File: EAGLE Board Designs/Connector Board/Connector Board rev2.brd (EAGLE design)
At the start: 109.2 x 45.7 mm, 51 parts, among them J1 CONNECTOR-8_μF_T_V_BLACK, J10 CONNECTOR-16_MF_T_V_, J11 CONNECTOR-18_MF_T_V_, J12 CONNECTOR-8_μF_T_V_BLACK, J2 CONNECTOR-8_μF_T_V_BLACK, J3 CONNECTOR-8_μF_T_V_BLACK, J4 CONNECTOR-10_MF_T_V_, J5 CONNECTOR-4_μF_T_V_BLACK, J6 CONNECTOR-24_CONNECTOR-24_, J7 CONNECTOR-24_CONNECTOR-24_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

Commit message: awaiting sab connections
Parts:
- removed R1, R2, R3: RESISTOR_0603_100, HyTechDevices:0603-RES
- removed R14, R15: RESISTOR_0603_100K, HyTechDevices:0603-RES
- removed TP3, TP4: TEST_POINT, HyTechDevices:5015
- added J13: CONNECTOR-2_MF_T_V_, HyTechDevices - Copy:MOLEX_MICROFIT_PTH_VERTICAL_02_SINGLE
- added JP1, JP2: JUMPER_0603_, HyTechDevices:0603-RES
- J1: value CONNECTOR-8_μF_T_V_BLACK -> CONNECTOR-6_μF_T_V_BLACK; device HyTechDevices:MOLEX_MICROFIT_PTH_VERTICAL_08_DUAL -> HyTechDevices:MOLEX_MICROFIT_PTH_VERTICAL_06_DUAL
- J4: value CONNECTOR-10_MF_T_V_ -> CONNECTOR-2_MF_T_V_; device HyTechDevices:MOLEX_MICROFIT_PTH_VERTICAL_10_DUAL -> HyTechDevices - Copy:MOLEX_MICROFIT_PTH_VERTICAL_02_SINGLE
- moved TP6 92.2 mm to (-12.1, -37.5), turned to 0 degrees
- moved TP5 86.8 mm to (-12.1, -33.7), turned to 0 degrees
- moved TP2 76.7 mm to (-12.1, -29.8), turned to 0 degrees
- moved TP1 71.4 mm to (-12.1, -26.0), turned to 0 degrees
- moved J4 60.3 mm to (-11.4, -45.1)
- moved J1 39.8 mm to (-10.2, -17.1), turned to 0 degrees
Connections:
- net SPN_POT_3_EXT renamed FR_CORNER_EXT_P
- removed net !STEERING_2_CS: J1.5
- removed net BRAKE_PRESSURE_F_EXT: J4.6, R14.1
- removed net BRAKE_PRESSURE_R_EXT: J4.7, R15.1
- removed net CANH_1: J10.3, TP3.1
- removed net CANL_1: J10.4, TP4.1
- removed net ECU_CLK: R1.2
- removed net ECU_SDI: R2.2
- removed net ECU_SDO: R3.2
- removed net INERTIA_SENSE_EXT: J7.5
- removed net LOAD_FL_EXT: J2.2
- removed net LOAD_FR_EXT: J3.2
- removed net LOAD_RL_EXT: J11.9
- removed net N$1: J1.2, R1.1
- removed net N$2: J1.3, R2.1
- removed net N$3: J1.4, R3.1
- removed net SPN_POT_1_EXT: J2.3
- removed net SPN_POT_2_EXT: J2.4
- removed net SPN_POT_4_EXT: J11.8
- removed net SPN_POT_5_EXT: J11.7
- new net CB_VIN: J2.1, J3.1, JP1.2, JP2.2
- net +12V: now also JP2.1
- net +24V: now also J10.1, JP1.1; no longer J2.1, J3.1
- net +5V: now also J2.2, J3.2; no longer J4.1
- net ACCEL_1_EXT: now also J1.2; no longer J4.2
- net ACCEL_2_EXT: now also J1.3; no longer J4.3
- net BMS_OK: now also J10.11; no longer J10.10
- net BRAKELIGHT_12V: no longer J10.15
- net BRAKE_1_EXT: now also J1.4; no longer J4.4
- net BRAKE_2_EXT: now also J1.5; no longer J4.5
- net CANH_2: now also J10.2; no longer J10.1
- net CANH_3: now also J10.5; no longer J10.6
- net CANL_2: now also J10.3; no longer J10.2
- net CANL_3: now also J10.4; no longer J10.5
- net CURRENT_EXT: now also J10.9; no longer J10.8
- net FL_CORNER_EXT_N: now also J2.4
- net FL_CORNER_EXT_P: now also J2.3
- net FR_CORNER_EXT_N: now also J3.4
- net GND: now also J1.6, J13.1, J4.1; no longer J1.8, J11.4, J11.5, J4.8, R14.2, R15.2
- net INVERTER_24V_EN_BOOSTED: now also J10.12; no longer J10.11
- net INVERTER_EN_BOOSTED: now also J10.13; no longer J10.12
- net LATCH_BTN: now also J10.15; no longer J10.14
- net OKHS_IN: now also J10.10; no longer J10.9
- net REFERENCE_EXT: now also J10.8; no longer J10.7
- net SHDN_I: now also J8.1, J8.2
- net SHDN_J: now also J8.3, J8.4, J9.1, J9.2; no longer J11.11, J11.16
- net SHDN_K: now also J10.6, J9.3, J9.4; no longer J8.1, J8.2
- net SHDN_L: now also J7.5; no longer J8.3, J8.4, J9.1, J9.2
- net SHDN_M: now also J10.14, J10.7; no longer J10.13, J9.3, J9.4
- net STEERING_1_EXT: no longer J1.7
- net THERM_FL_EXT: now also J13.2
- net THERM_FR_EXT: now also J4.2
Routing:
- net BRAKE_2_EXT: track 109.8 -> 0.00 mm
- net STEERING_1_EXT: track 105.8 -> 0.00 mm
- net ACCEL_2_EXT: track 105.8 -> 0.00 mm
- net +5V: track 104.0 -> 0.00 mm, vias 1 -> 0
- net BRAKE_1_EXT: track 100.7 -> 0.00 mm
- net ACCEL_1_EXT: track 96.7 -> 0.00 mm
- net BRAKE_PRESSURE_F_EXT: track 85.2 -> 0.00 mm
- net BRAKE_PRESSURE_R_EXT: track 80.9 -> 0.00 mm
- net LOAD_FR_EXT: track 73.8 -> 0.00 mm
- net SHDN_L: track 87.6 -> 19.4 mm, vias 3 -> 0
- net SHDN_I: track 85.0 -> 152.6 mm, vias 3 -> 6
- net FR_CORNER_EXT_P: track 65.9 -> 0.00 mm
- net SPN_POT_2_EXT: track 60.5 -> 0.00 mm
- net LOAD_FL_EXT: track 52.7 -> 0.00 mm
- net SPN_POT_1_EXT: track 50.1 -> 0.00 mm
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
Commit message: shdn updates
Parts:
- J10: value CONNECTOR-16_MF_T_V_ -> CONNECTOR-18_MF_T_V_; device HyTechDevices:MOLEX_MICROFIT_PTH_VERTICAL_16_DUAL -> HyTechDevices:MOLEX_MICROFIT_PTH_VERTICAL_18_DUAL
- J11: value CONNECTOR-18_MF_T_V_ -> CONNECTOR-6_μF_T_V_BLACK; device HyTechDevices:MOLEX_MICROFIT_PTH_VERTICAL_18_DUAL -> HyTechDevices:MOLEX_MICROFIT_PTH_VERTICAL_06_DUAL
- moved J11 148.2 mm to (-10.2, -88.3), turned to 0 degrees
- moved J10 107.2 mm to (-0.64, -74.3), turned to 0 degrees
- moved TP1 72.4 mm to (-14.6, -98.4)
- moved TP2 72.4 mm to (-14.6, -102.2)
- moved TP5 72.4 mm to (-14.6, -106.0)
- moved TP6 72.4 mm to (-14.6, -109.9)
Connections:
- removed net LOAD_RR_EXT: J11.14
- removed net SPN_POT_6_EXT: J11.15
- new net N$2: J10.5
- new net N$3: J10.6
- net +24V: now also J11.3, J11.4, J11.5; no longer J10.1, J11.13, J11.2, J11.6
- net BMS_OK: now also J10.12; no longer J10.11
- net BRAKELIGHT_12V: now also J10.15
- net CANH_2: now also J10.1; no longer J10.2
- net CANH_3: now also J10.4; no longer J10.5
- net CANL_2: now also J10.2; no longer J10.3
- net CANL_3: now also J10.3; no longer J10.4
- net CURRENT_EXT: now also J10.10; no longer J10.9
- net GND: now also J10.18, J11.2, J11.6; no longer J10.16, J11.12, J11.18, J11.3
- net INVERTER_24V_EN_BOOSTED: now also J10.13; no longer J10.12
- net INVERTER_EN_BOOSTED: now also J10.14; no longer J10.13
- net LATCH_BTN: now also J10.16; no longer J10.15
- net OKHS_IN: now also J10.11; no longer J10.10
- net REFERENCE_EXT: now also J10.9; no longer J10.8
- net SHDN_I: no longer J11.10
- net SHDN_K: now also J10.7; no longer J10.6, J11.17
- net SHDN_M: now also J10.17, J10.8; no longer J10.14, J10.7
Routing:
- net +24V: track 193.8 -> 156.1 mm
- net SHDN_K: track 67.9 -> 43.4 mm
- net LOAD_RR_EXT: track 19.1 -> 0.00 mm
- net SPN_POT_6_EXT: track 12.9 -> 0.00 mm
- net SHDN_I: track 152.6 -> 140.9 mm

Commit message: finalized schem
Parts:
- added J14: CONNECTOR-8_μF_T_V_BLACK, HyTechDevices:MOLEX_MICROFIT_PTH_VERTICAL_08_DUAL
- J11: value CONNECTOR-6_μF_T_V_BLACK -> CONNECTOR-8_μF_T_V_BLACK; device HyTechDevices:MOLEX_MICROFIT_PTH_VERTICAL_06_DUAL -> HyTechDevices:MOLEX_MICROFIT_PTH_VERTICAL_08_DUAL
- JP1, JP2: device HyTechDevices:0603-RES -> HyTechDevices:0603-RES@1
- moved J11 50.8 mm to (-8.26, -139.1)
- moved TP5 21.6 mm to (-14.6, -127.6)
- moved TP6 21.6 mm to (-14.6, -131.4)
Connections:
- removed net RS422_RX_N: J6.14
- removed net RS422_RX_P: J6.13
- removed net RS422_TX_N: J6.10
- removed net RS422_TX_P: J6.9
- new net STEERING_2_EXT: J14.6, J7.20
- new net STEERING_RX_N: J14.5, J6.14
- new net STEERING_RX_P: J14.4, J6.13
- new net STEERING_TX_N: J14.3, J6.10
- new net STEERING_TX_P: J14.2, J6.9
- net +24V: now also J11.7; no longer J11.4
- net +5V: now also J14.1
- net BMS_OK: now also J10.13; no longer J10.12
- net BRAKELIGHT_12V: now also J10.16; no longer J10.15
- net CANH_3: now also J10.8; no longer J10.4
- net CANL_3: now also J10.7; no longer J10.3
- net CURRENT_EXT: now also J10.11; no longer J10.10
- net GND: now also J11.4, J11.8, J14.8
- net INVERTER_24V_EN_BOOSTED: now also J10.14; no longer J10.13
- net INVERTER_EN_BOOSTED: now also J10.15; no longer J10.14
- net LATCH_BTN: now also J10.17; no longer J10.16
- net OKHS_IN: now also J10.12; no longer J10.11
- net REFERENCE_EXT: now also J10.10; no longer J10.9
- net SHDN_K: now also J10.3, J10.4; no longer J10.7
- net SHDN_M: no longer J10.17, J10.8
- net STEERING_1_EXT: now also J14.7

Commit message: schem review
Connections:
- removed net SHDN_M: J12.2
- net SHDN_J: now also J12.6
- net SHDN_K: now also J12.2
- net SHDN_L: no longer J12.6
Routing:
- net SHDN_K: track 43.4 -> 70.7 mm
- net SHDN_M: track 27.3 -> 0.00 mm
- net SHDN_L: track 19.4 -> 0.00 mm
- net SHDN_J: track 63.7 -> 83.1 mm
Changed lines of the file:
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@@
 <contactref element="J10" pad="3"/>
 <contactref element="J10" pad="4"/>
-<wire x1="5.365" y1="-77.295" x2="2.365" y2="-77.295" width="0" layer="19" extent="1-1"/>
-<wire x1="70.8914" y1="7.62" x2="5.365" y2="-77.295" width="0" layer="19" extent="1-1"/>
-</signal>
-<signal name="SHDN_L">
-<contactref element="J12" pad="6"/>
-<wire x1="99.06" y1="12.4714" x2="100.5586" y2="13.97" width="0.254" layer="16"/>
-<wire x1="85.598" y1="7.62" x2="86.36" y2="6.858" width="0.254" layer="16"/>
-<wire x1="86.36" y1="6.858" x2="95.504" y2="6.858" width="0.254" layer="16"/>
-<wire x1="95.504" y1="6.858" x2="99.06" y2="10.414" width="0.254" layer="16"/>
-<wire x1="99.06" y1="10.414" x2="99.06" y2="12.4714" width="0.254" layer="16"/>
-<contactref element="J7" pad="5"/>
-<wire x1="9.51356875" y1="-19.414490625" x2="85.598" y2="7.62" width="0" layer="19" extent="16-16"/>
-</signal>
-<signal name="SHDN_M">
 <contactref element="J12" pad="2"/>
 <wire x1="100.5586" y1="10.7188" x2="95.9358" y2="6.096" width="0.254" layer="16"/>
 <wire x1="100.5586" y1="10.7188" x2="100.5586" y2="10.9728" width="0.254" layer="16"/>
 <wire x1="75.4126" y1="6.096" x2="95.9358" y2="6.096" width="0.254" layer="16"/>
+<wire x1="73.8886" y1="7.62" x2="75.4126" y2="6.096" width="0" layer="19" extent="16-16"/>
+<wire x1="5.365" y1="-77.295" x2="70.8914" y2="7.62" width="0" layer="19" extent="1-1"/>
+<wire x1="2.365" y1="-77.295" x2="5.365" y2="-77.295" width="0" layer="19" extent="1-1"/>
+</signal>
+<signal name="SHDN_L">
+<contactref element="J7" pad="5"/>
 </signal>
 <signal name="+12V">
@@
 <wire x1="57.912" y1="23.876" x2="65.532" y2="16.256" width="0.254" layer="2"/>
 <wire x1="69.596" y1="12.192" x2="69.596" y2="5.9182" width="0.254" layer="2"/>
+<contactref element="J12" pad="6"/>
+<wire x1="99.06" y1="12.4714" x2="100.5586" y2="13.97" width="0.254" layer="16"/>
+<wire x1="85.598" y1="7.62" x2="86.36" y2="6.858" width="0.254" layer="16"/>
+<wire x1="86.36" y1="6.858" x2="95.504" y2="6.858" width="0.254" layer="16"/>
+<wire x1="95.504" y1="6.858" x2="99.06" y2="10.414" width="0.254" layer="16"/>
+<wire x1="99.06" y1="10.414" x2="99.06" y2="12.4714" width="0.254" layer="16"/>
+<wire x1="85.3186" y1="7.62" x2="85.598" y2="7.62" width="0" layer="19" extent="16-16"/>
 <wire x1="79.3242" y1="4.6228" x2="82.3214" y2="7.62" width="0" layer="19" extent="1-1"/>
 </signal>

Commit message: initiial layout
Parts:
- moved J11 177.3 mm to (76.8, 16.5)
- moved J14 134.3 mm to (7.62, 15.9), turned to 270 degrees
- moved J10 115.9 mm to (51.4, 29.2), turned to 180 degrees
- moved JP1 104.1 mm to (-14.6, 40.6)
- moved JP2 104.1 mm to (-14.6, 37.5)
- moved TP1 104.1 mm to (-14.6, 5.71)
- moved TP2 104.1 mm to (-14.6, 1.91)
- moved TP5 104.1 mm to (-14.6, -23.5)
- moved TP6 104.1 mm to (-14.6, -27.3)
- moved J13 83.8 mm to (40.0, 9.65)
- moved J7 80.1 mm to (70.6, 40.6)
- moved J4 64.3 mm to (22.6, 9.53)
- moved J6 51.2 mm to (26.9, 40.6)
- moved U$11 42.7 mm to (85.2, 2.54), flipped to the top, turned to 90 degrees
- moved J12 40.1 mm to (59.1, 16.5)
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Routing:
- net +24V: track 156.1 -> 0.00 mm
- net SHDN_I: track 140.9 -> 0.00 mm, vias 6 -> 0
- net SHDN_B: track 116.3 -> 0.00 mm, vias 2 -> 0
- net SHDN_J: track 83.1 -> 0.00 mm, vias 3 -> 0
- net CANL_3: track 73.7 -> 0.00 mm
- net CANH_3: track 71.7 -> 0.00 mm
- net SHDN_K: track 70.7 -> 0.00 mm
- net BRAKELIGHT_EN: track 62.4 -> 0.00 mm
- net SHDN_H: track 59.4 -> 0.00 mm, vias 1 -> 0
- net INVERTER_EN: track 51.2 -> 0.00 mm, vias 2 -> 0
- net SHDN_A: track 43.9 -> 0.00 mm
- net +12V: track 23.5 -> 0.00 mm
- net INVERTER_24V_EN: track 16.9 -> 0.00 mm
- net INVERTER_24V_EN_BOOSTED: track 8.97 -> 0.00 mm
- net N$8: track 5.65 -> 0.00 mm
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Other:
- board size 109.2 x 45.7 mm -> 97.5 x 50.8 mm
- board text added: "Connector Board Rev 2 Designed by Siddharth Lohani"
- board text added: "DASH?"
- board text added: "FL_THERM"
- board text added: "FR_THERM"
- board text added: "Power"
- board text removed: "Connector Board rev1 Designed by Mikhail Allen"
- board text removed: "DASH"
- board text removed: "FIREWALL"
- board text removed: "FL CORNER"
- board text removed: "FR CORNER"

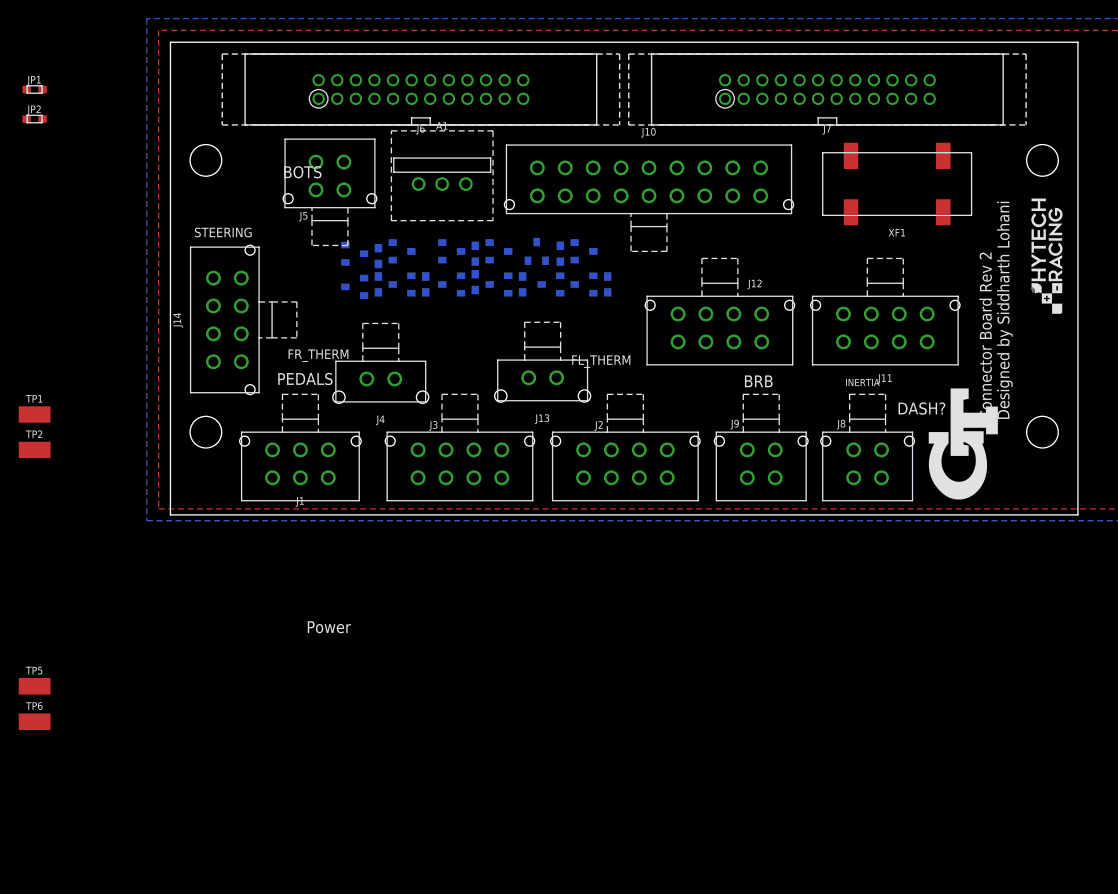
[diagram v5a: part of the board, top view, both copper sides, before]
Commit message: new layout with expanded pedal connector
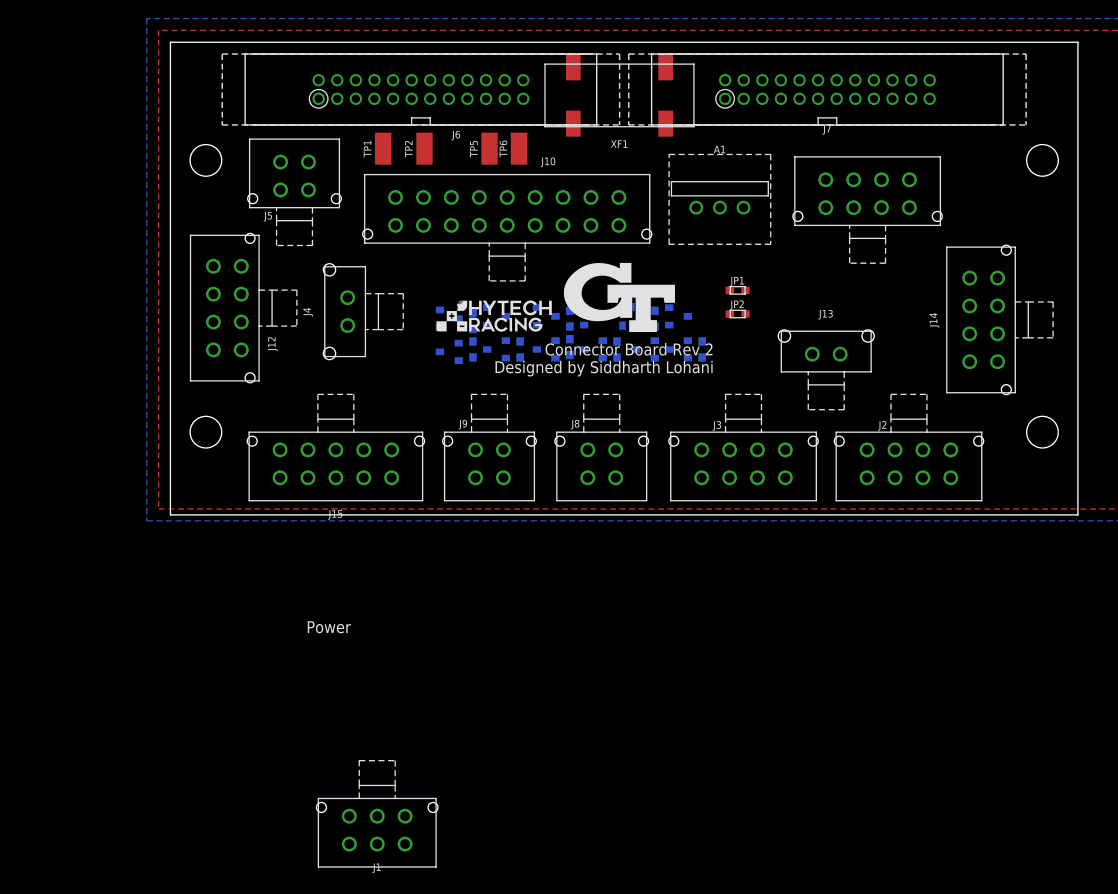
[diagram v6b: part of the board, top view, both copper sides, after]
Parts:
- added J15: CONNECTOR-10_MF_T_V_, HyTechDevices:MOLEX_MICROFIT_PTH_VERTICAL_10_DUAL
- moved J14 81.3 mm to (88.9, 15.9)
- moved TP6 80.7 mm to (37.5, 34.3), turned to 90 degrees
- moved JP1 78.6 mm to (61.0, 19.1)
- moved JP2 78.4 mm to (61.0, 16.5)
- moved TP5 75.7 mm to (34.3, 34.3), turned to 90 degrees
- moved U$14 67.3 mm to (28.6, 14.6), turned to 0 degrees
- moved TP2 53.0 mm to (27.3, 34.3), turned to 90 degrees
- moved J12 51.4 mm to (7.62, 17.1), turned to 270 degrees
- moved TP1 47.1 mm to (22.9, 34.3), turned to 90 degrees
- moved J1 40.2 mm to (22.2, -37.5)
- moved U$11 40.2 mm to (48.3, 18.3), turned to 0 degrees
- moved XF1 31.3 mm to (48.3, 40.0)
- moved J13 30.6 mm to (70.5, 12.2), turned to 180 degrees
- moved J3 30.5 mm to (61.6, 1.91)
- moved J2 30.5 mm to (79.4, 1.91)
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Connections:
- new net N$10: J15.4
- new net N$12: J15.5
- new net N$13: J15.6
- new net N$14: J15.7
- new net N$15: J15.8
- new net N$6: J15.3
- net +5V: now also J15.1, J15.2
- net GND: now also J15.10, J15.9
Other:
- board text removed: "BOTS"
- board text removed: "BRB"
- board text removed: "DASH?"
- board text removed: "FL_THERM"
- board text removed: "FR_THERM"
- board text removed: "INERTIA"
- board text removed: "PEDALS"
- board text removed: "STEERING"
